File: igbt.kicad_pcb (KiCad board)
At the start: 2 copper layers, 38 parts, among them J1 A_Top, J2 A_Bottom, J3 B_Top, J4 B_Bottom, J5 C_Top, J6 C_Bottom, J7 Sense_AC_B, J8 Sense_AC_A, J9 DC_Sense, Q1 IRG4PF50W, Q2 IRG4PF50W, Q3 IRG4PF50W, Q4 IRG4PF50W, Q5 IRG4PF50W, Q6 IRG4PF50W, U1 ACS758xCB-050B-PFF, U2 ACS758xCB-050B-PFF

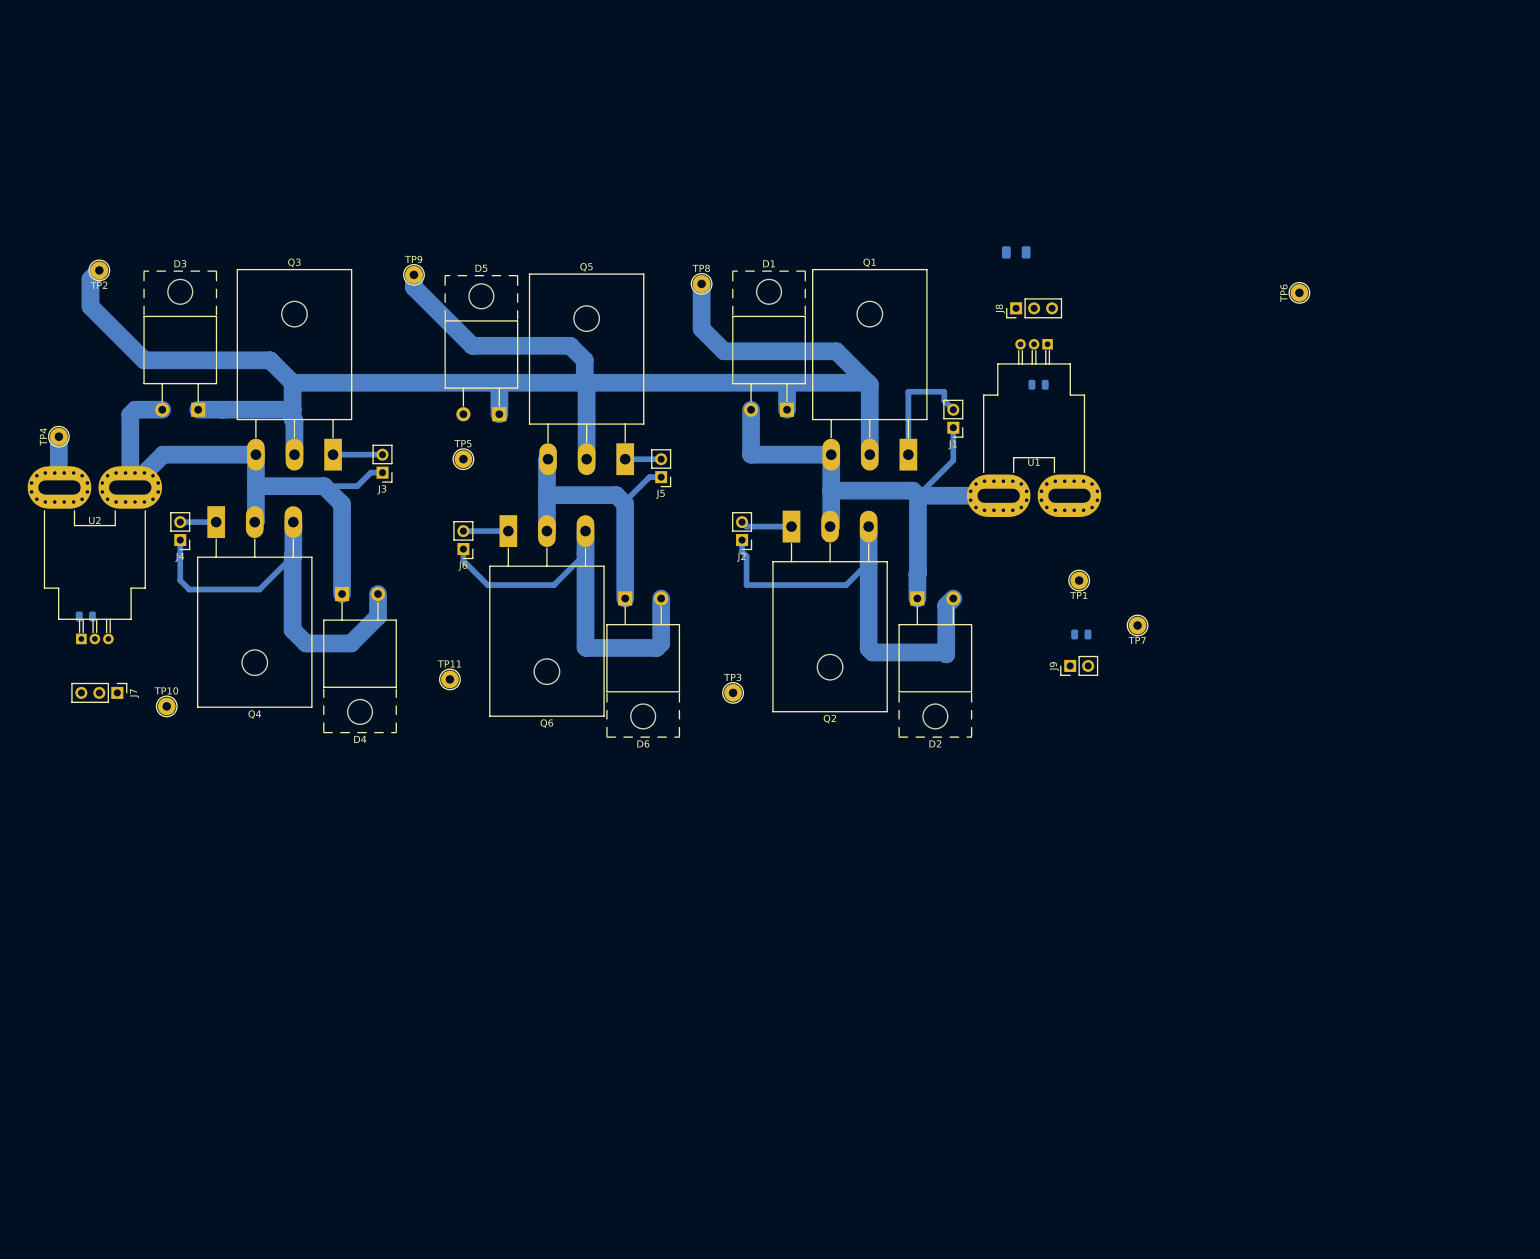
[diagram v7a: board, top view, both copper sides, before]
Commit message: 160x100mm size
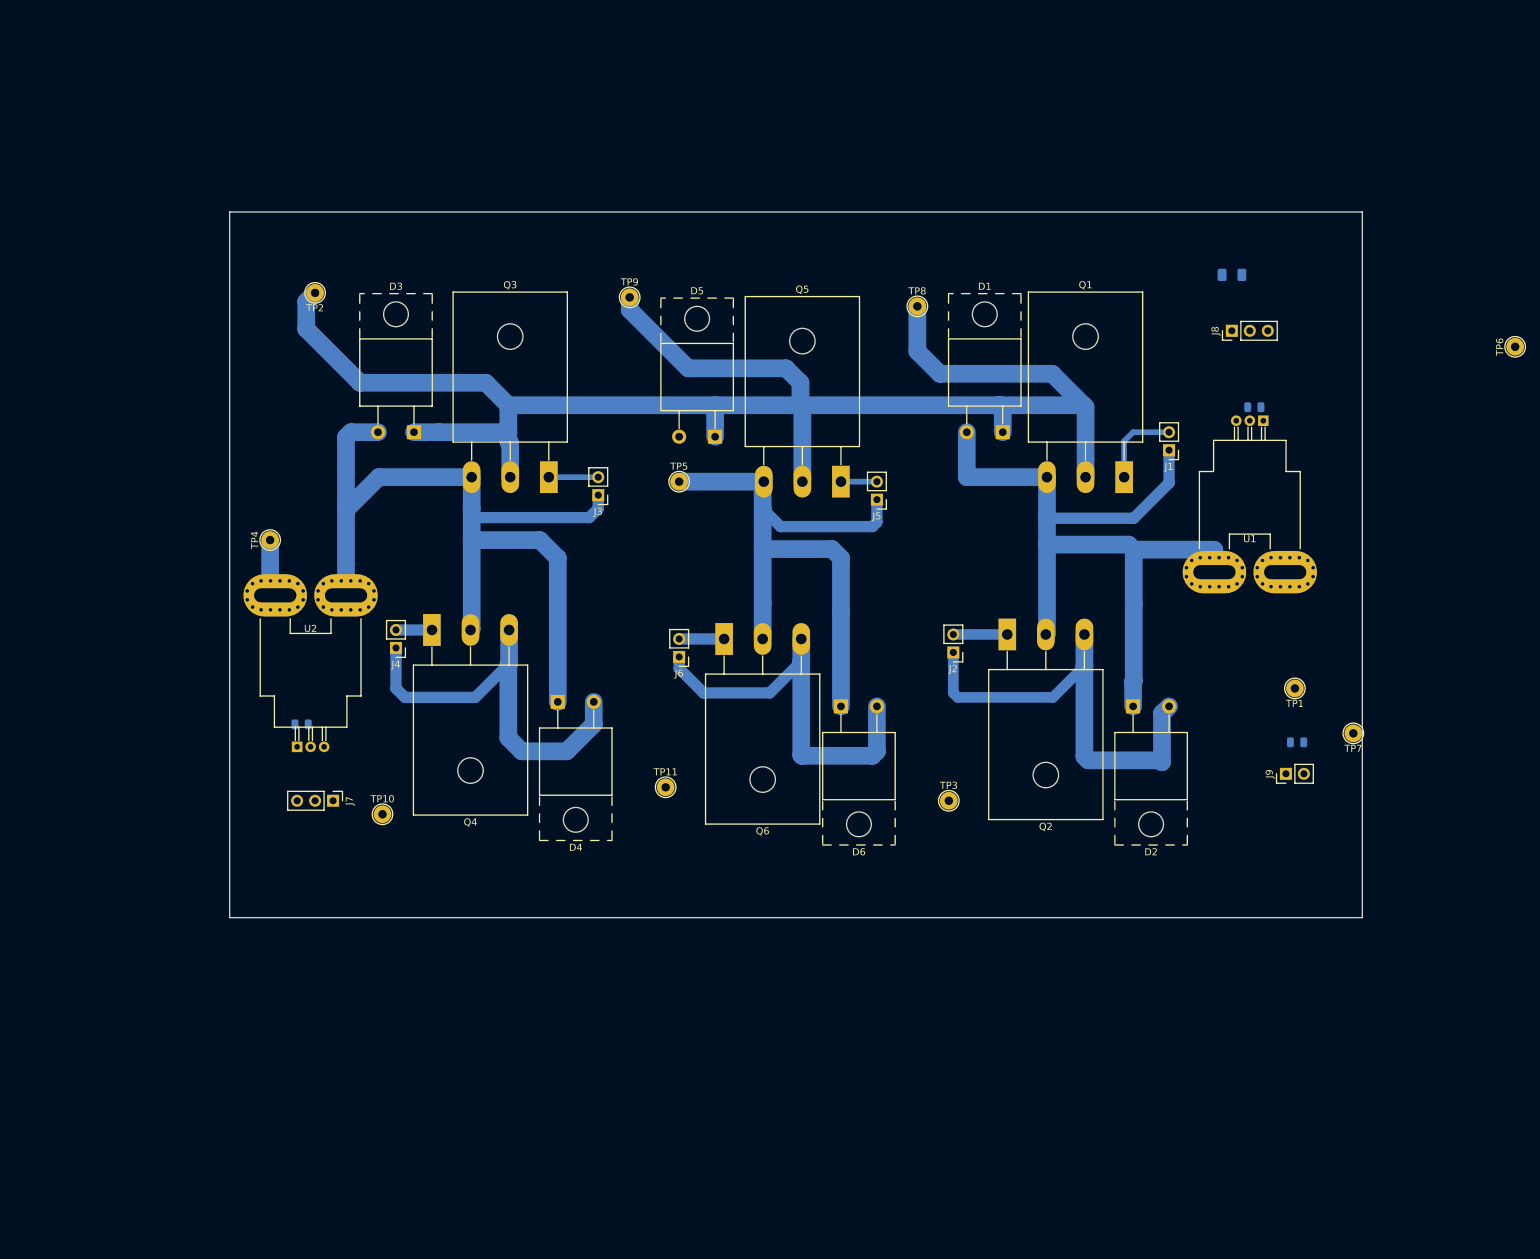
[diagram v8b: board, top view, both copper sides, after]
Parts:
- moved TP1 34.1 mm to (214.0, 113.7)
- moved D6 34.1 mm to (149.9, 116.2)
- moved R8 34.1 mm to (214.3, 121.3)
- moved C5 34.1 mm to (73.7, 118.7)
- moved J4 34.1 mm to (87.0, 108.0)
- moved TP11 34.1 mm to (125.1, 127.6)
- moved D4 34.1 mm to (109.9, 115.6)
- moved J6 34.1 mm to (127.0, 109.2)
- moved J7 34.1 mm to (78.1, 129.5)
- moved Q4 34.1 mm to (92.1, 105.4)
- moved TP10 34.1 mm to (85.1, 131.4)
- moved U2 34.1 mm to (73.0, 121.9)
- moved D2 34.1 mm to (191.1, 116.2)
- moved J9 34.1 mm to (212.7, 125.7)
- moved Q2 34.1 mm to (173.4, 106.0)
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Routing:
- net Net-(D5-Pad2): track 42.0 -> 88.1 mm
- net Net-(D3-Pad2): track 79.3 -> 122.9 mm
- net Net-(D1-Pad2): track 90.5 -> 122.6 mm
- net Net-(J1-Pad2): track 17.0 -> 12.0 mm
- net Net-(D2-Pad2): track 175.0 -> 176.2 mm
- net Net-(TP4-Pad1): track 7.21 -> 8.11 mm
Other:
- board outline added: 160 x 99.7 mm
